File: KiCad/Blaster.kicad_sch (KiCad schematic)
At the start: 28 parts, among them Q1 BUK9832-55A, Q2 BUK9832-55A, SW2 Fire, SW3 Freq Select, SW4 Fire Select, U2 PIC16F1788-IP, U3 Audio Board

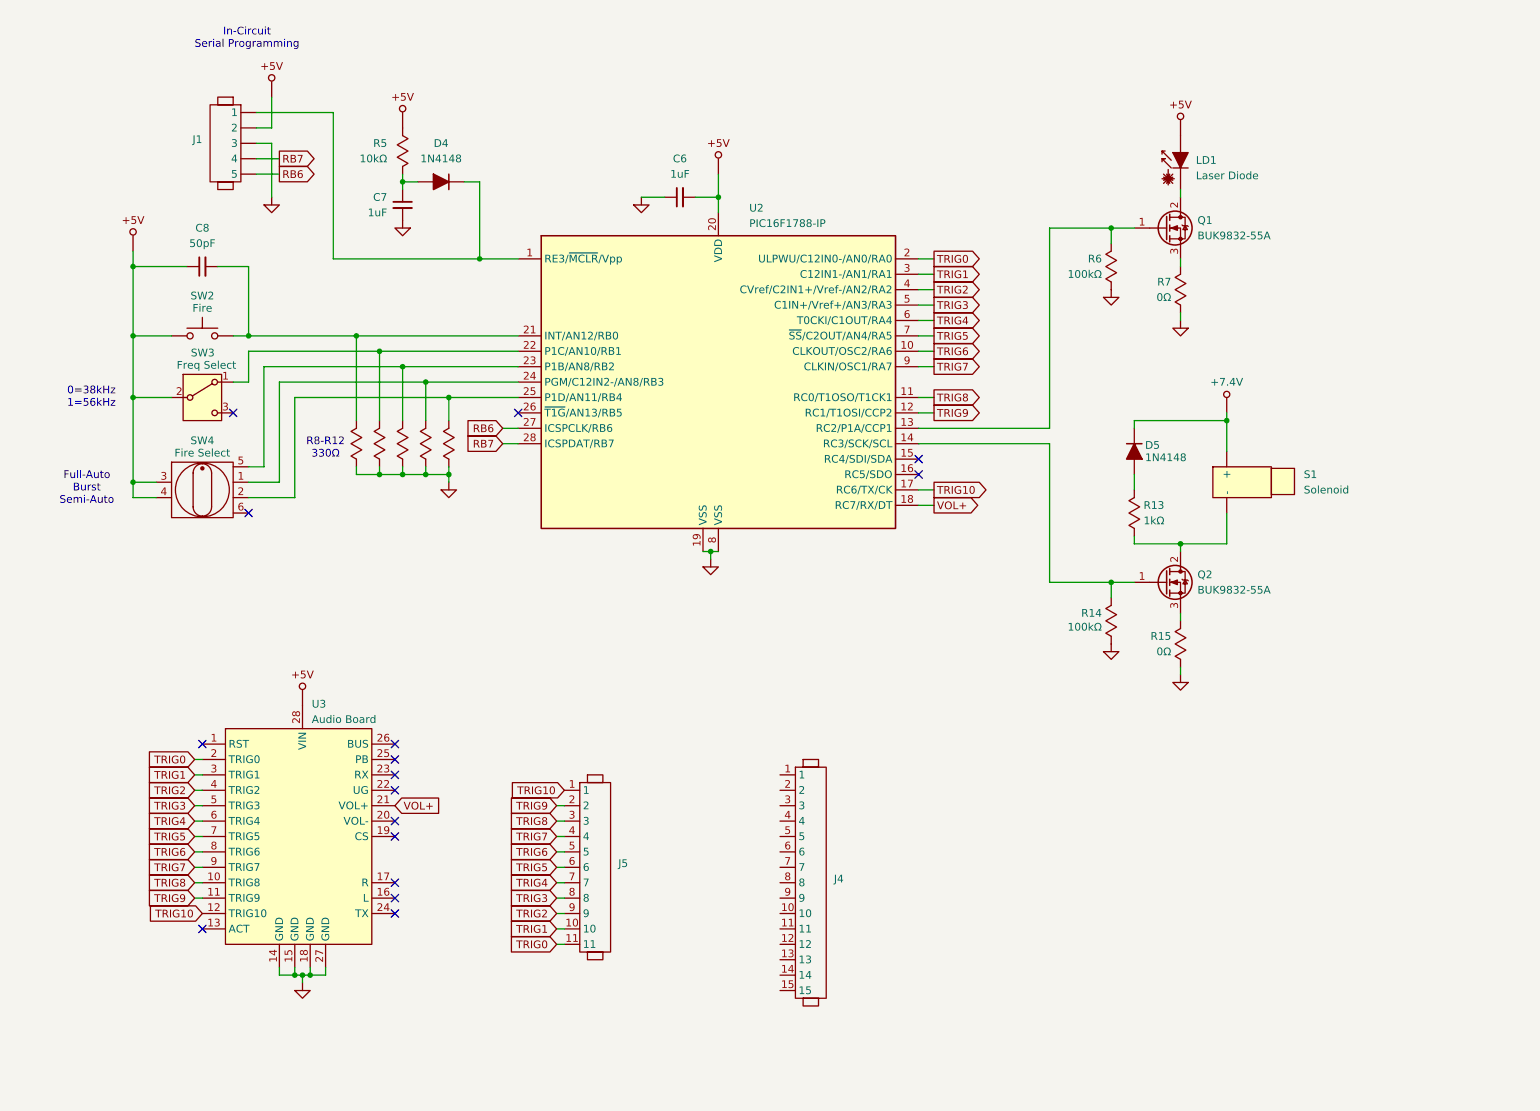
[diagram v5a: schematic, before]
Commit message: recovered some lost parts of the schematic, still needs a bit of work to get back
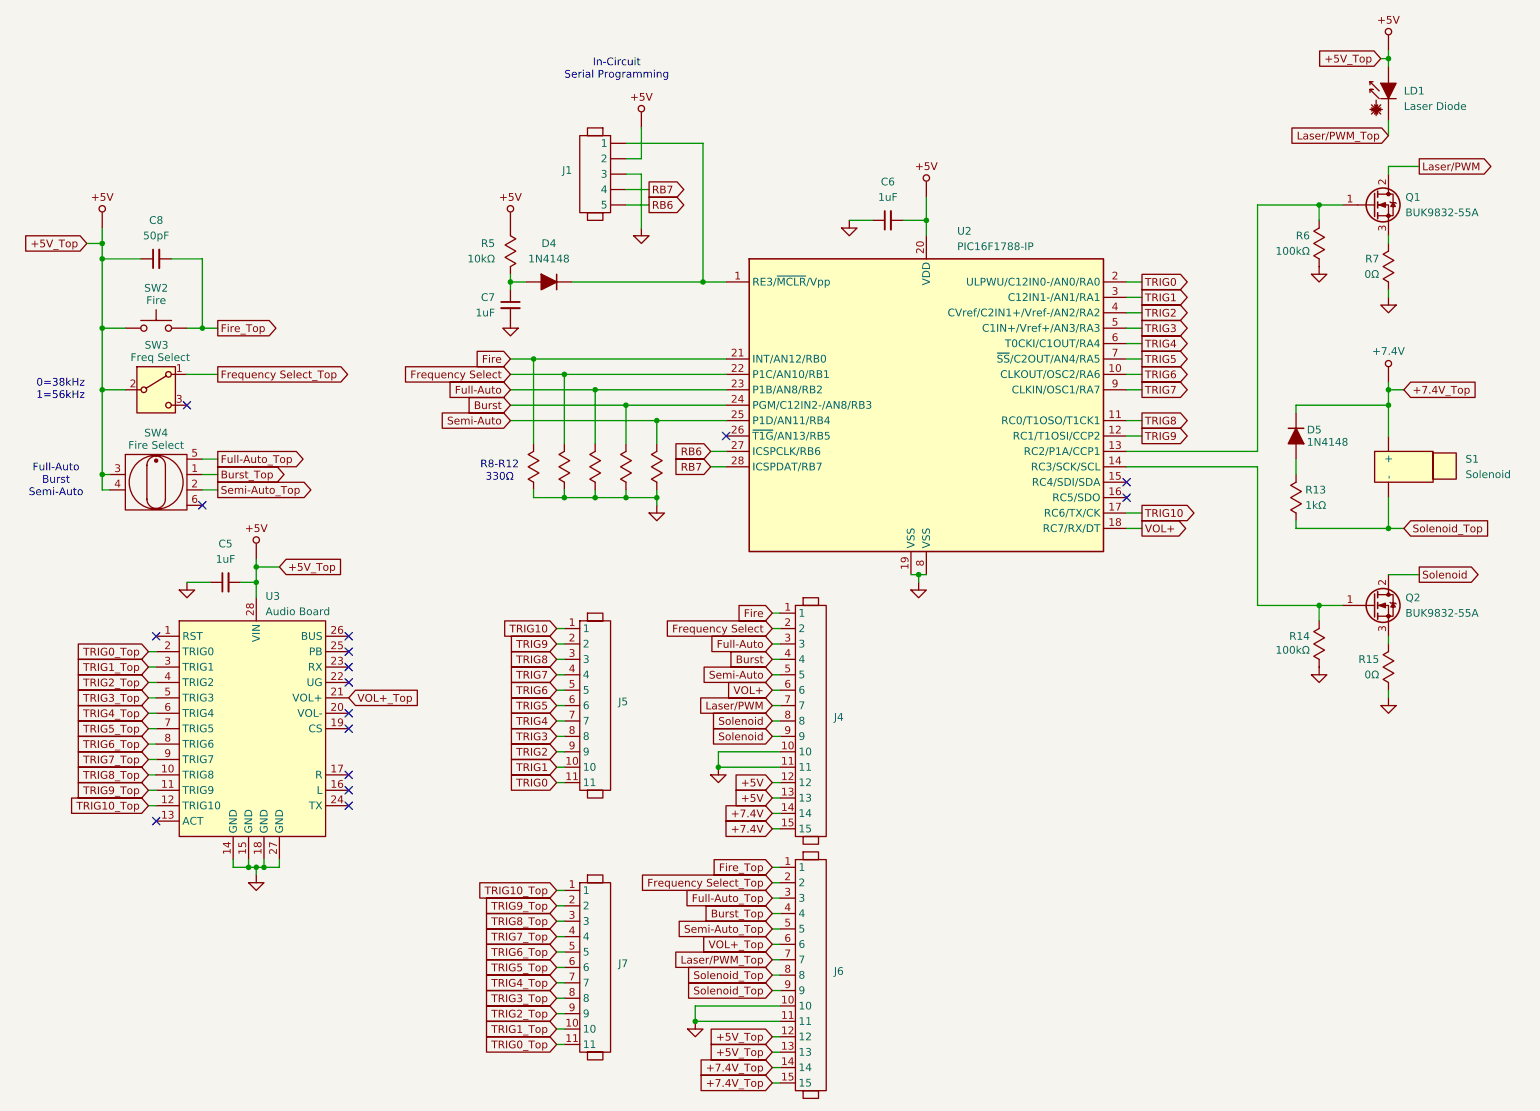
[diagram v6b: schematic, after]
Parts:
- added C5: 1uF, Capacitor_SMD:C_0805_2012Metric_Pad1.18x1.45mm_HandSolder, symbol Device:C_Small
- added J6: ~, symbol Libraries:Header_1x15
- added J7: ~, symbol Libraries:Header_1x11
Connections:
- net +5V: now also J4.12, J4.13, C5.2, J6.12, J6.13
- net TRIG0: no longer U3.2 (TRIG0)
- net TRIG1: no longer U3.3 (TRIG1)
- net TRIG10: no longer U3.12 (TRIG10)
- net TRIG2: no longer U3.4 (TRIG2)
- net TRIG3: no longer U3.5 (TRIG3)
- net TRIG4: no longer U3.6 (TRIG4)
- net TRIG5: no longer U3.7 (TRIG5)
- net TRIG6: no longer U3.8 (TRIG6)
- net TRIG7: no longer U3.9 (TRIG7)
- net TRIG8: no longer U3.10 (TRIG8)
- net TRIG9: no longer U3.11 (TRIG9)
- net VOL+: now also J4.6; no longer U3.21 (VOL+)
- net Laser/PWM: now reaches Q1.2 (D)
- net Laser/PWM: now also J4.7; no longer LD1.2 (K)
- net Fire: now reaches R8.1, U2.21 (INT/AN12/RB0)
- net Fire: now also J4.1; no longer C8.2, SW2.2
- net Burst: now reaches R11.1, U2.24 (PGM/C12IN2-/AN8/RB3)
- net Burst: now also J4.4; no longer SW4.1
- net Semi-Auto: now reaches R12.1, U2.25 (P1D/AN11/RB4)
- net Semi-Auto: now also J4.5; no longer SW4.2
- net Full-Auto: now reaches R10.1, U2.23 (P1B/AN8/RB2)
- net Full-Auto: now also J4.3; no longer SW4.5
- net Frequency Select: now reaches R9.1, U2.22 (P1C/AN10/RB1)
- net Frequency Select: now also J4.2; no longer SW3.1 (A)
- net Solenoid_Top: now reaches R13.1, S1.2 (-)
- net Solenoid_Top: now also J6.8, J6.9; no longer Q2.2 (D)
- net +7.4V_Top: now reaches D5.1 (K), S1.1 (+)
- net +7.4V_Top: now also J6.14, J6.15
- net at J4.10: now also J4.11
- net +7.4V: now reaches J4.14
- net +7.4V: now also J4.15
- net Solenoid: now reaches J4.8
- net Solenoid: now also J4.9, Q2.2 (D)
- new net: J6.10, J6.11
- new net Burst_Top: J6.4, SW4.1
- new net Fire_Top: C8.2, J6.1, SW2.2
- new net Frequency Select_Top: J6.2, SW3.1 (A)
- new net Full-Auto_Top: J6.3, SW4.5
- new net Laser/PWM_Top: J6.7, LD1.2 (K)
- new net Semi-Auto_Top: J6.5, SW4.2
- new net TRIG0_Top: J7.11, U3.2 (TRIG0)
- new net TRIG10_Top: J7.1, U3.12 (TRIG10)
- new net TRIG1_Top: J7.10, U3.3 (TRIG1)
- new net TRIG2_Top: J7.9, U3.4 (TRIG2)
- new net TRIG3_Top: J7.8, U3.5 (TRIG3)
- new net TRIG4_Top: J7.7, U3.6 (TRIG4)
- new net TRIG5_Top: J7.6, U3.7 (TRIG5)
- new net TRIG6_Top: J7.5, U3.8 (TRIG6)
- new net TRIG7_Top: J7.4, U3.9 (TRIG7)
- new net TRIG8_Top: J7.3, U3.10 (TRIG8)
- new net TRIG9_Top: J7.2, U3.11 (TRIG9)
- new net VOL+_Top: J6.6, U3.21 (VOL+)
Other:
- moved on the sheet: C6, C7, C8, D4, D5, J1, J4, J5, LD1, Q1, Q2, R13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
